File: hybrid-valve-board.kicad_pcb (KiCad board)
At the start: 2 copper layers, 68 x 79 mm, 42 parts, among them J1 XV Supply, J10 ARM, J2 MCU Supply, J3 XV In, J4 XV In, J5 XV In, J6 Continuity, J7 XV Out, J8 XV Out, J9 XV Out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

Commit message: Warranty text
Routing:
- net /XV7_PWR: track 22.5 -> 25.6 mm

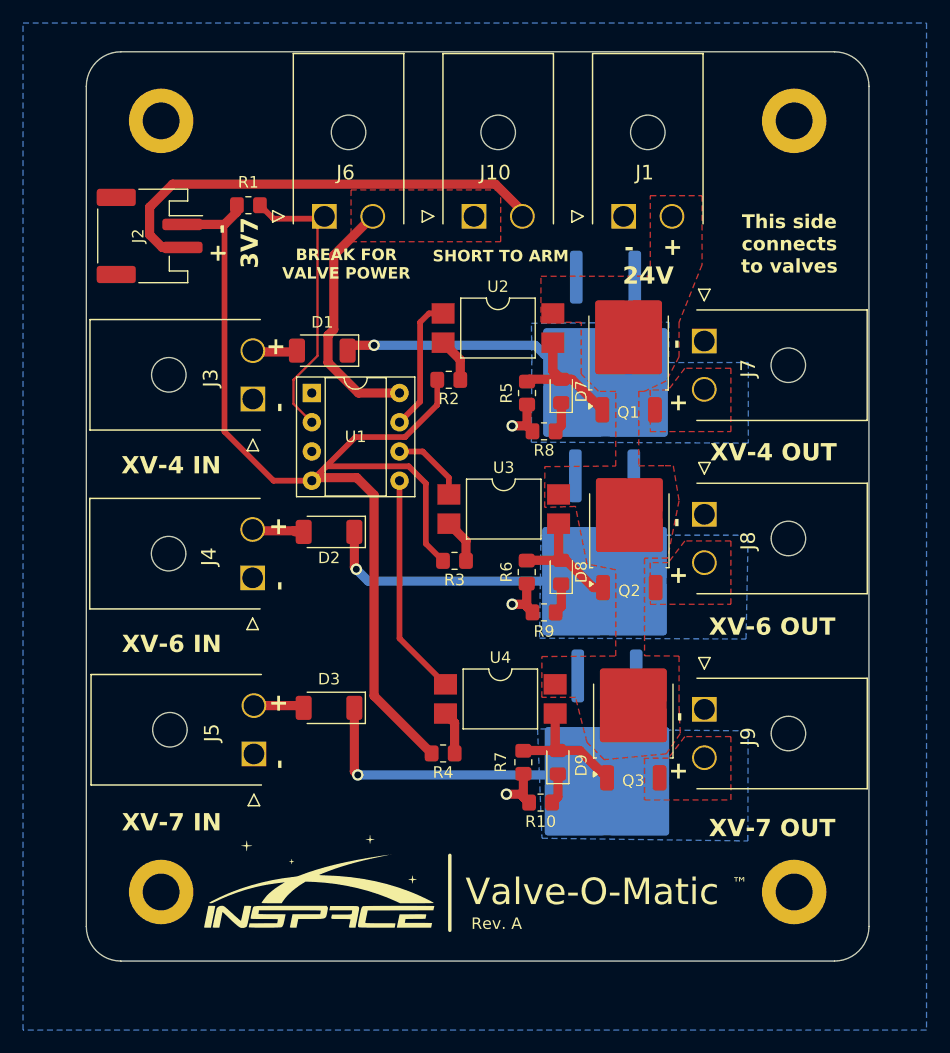
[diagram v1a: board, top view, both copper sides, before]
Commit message: Added: reverse polarity protection for MCU, arming LED and PMOS switching
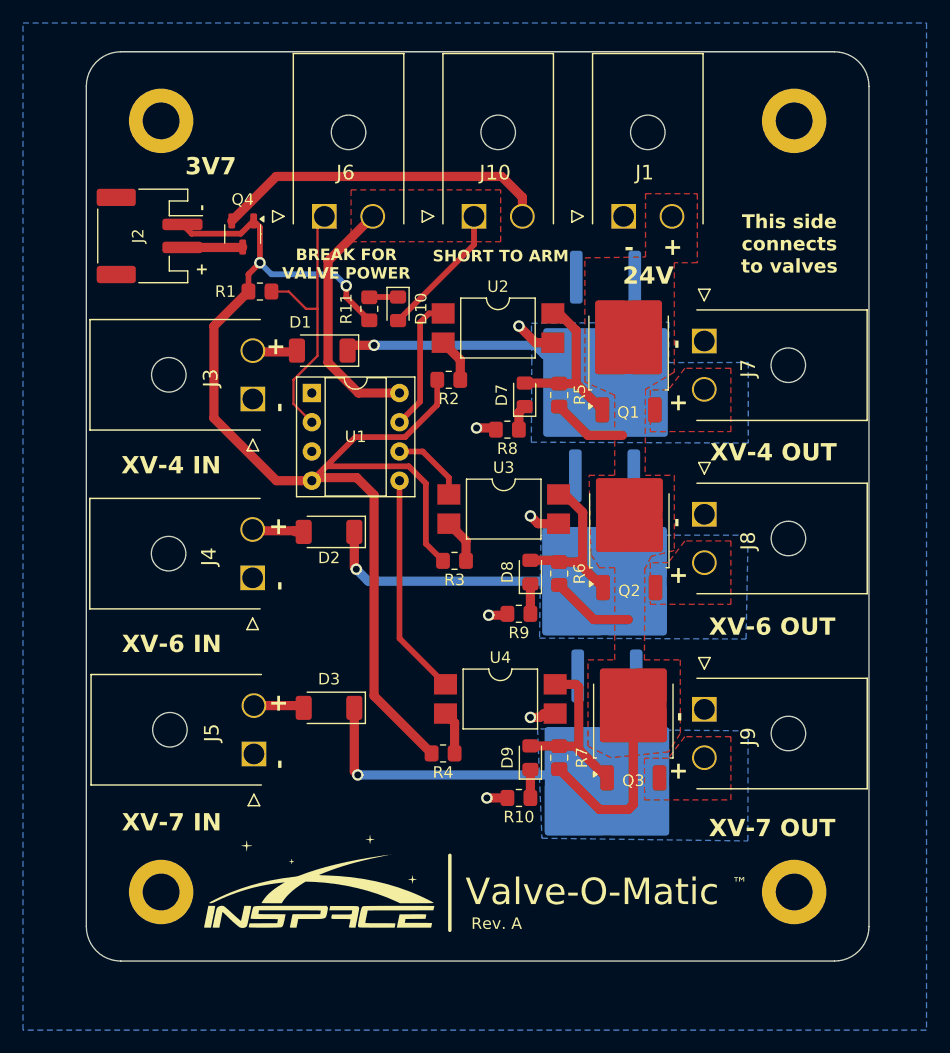
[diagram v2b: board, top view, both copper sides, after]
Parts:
- added D10: GREEN, LED_SMD:LED_0805_2012Metric_Pad1.15x1.40mm_HandSolder, F.Cu at (127.5, 86.5)
- added Q4: PMOS, Package_TO_SOT_SMD:SOT-23-3, F.Cu at (114.0, 80.0)
- added R11: 150R, Resistor_SMD:R_0805_2012Metric_Pad1.20x1.40mm_HandSolder, F.Cu at (125.0, 86.5)
- Q1, Q2, Q3: value NMOS -> PMOS
- moved R1 7.57 mm to (115.5, 85.0)
- moved D7 3.20 mm to (138.5, 94.0)
- moved R8 3.18 mm to (137.0, 97.0)
- moved R7 3.14 mm to (141.5, 125.5), turned to 90 degrees
- moved R6 2.82 mm to (141.5, 109.5), turned to 90 degrees
- moved R5 2.80 mm to (141.5, 94.0), turned to 90 degrees
- moved D8 2.68 mm to (139.0, 109.4)
- moved D9 2.42 mm to (139.0, 125.5)
- moved R9 2.18 mm to (138.0, 113.0)
- moved R10 1.93 mm to (138.0, 129.0)
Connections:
- J10 pad 2: VBAT -> VPROT
- R5 pad 1: /XV4_ON_24V -> +24VBAT
- R5 pad 2: GND -> /XV4_ON_24V
- R6 pad 1: /XV6_ON_24V -> +24VBAT
- R6 pad 2: GND -> /XV6_ON_24V
- R7 pad 1: /XV7_ON_24V -> +24VBAT
- R7 pad 2: GND -> /XV7_ON_24V
- U2 pad 3: /XV4_ON_24V -> GND
- U2 pad 4: +24VBAT -> /XV4_ON_24V
- U3 pad 3: /XV6_ON_24V -> GND
- U3 pad 4: +24VBAT -> /XV6_ON_24V
- U4 pad 3: /XV7_ON_24V -> GND
- U4 pad 4: +24VBAT -> /XV7_ON_24V
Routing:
- net VBAT: track 40.3 -> 5.25 mm
- net +24VBAT: track 0.00 -> 30.5 mm
- net VPROT: track 0.00 -> 29.7 mm
- net MCU_GND: track 98.0 -> 113.8 mm, vias 0 -> 2
- net +3V3: track 21.6 -> 33.4 mm
- net /XV6_ON_24V: track 10.9 -> 14.8 mm
- net /XV7_ON_24V: track 11.6 -> 15.4 mm
- net /XV4_ON_24V: track 11.2 -> 15.0 mm
- net Net-(D10-K): track 0.00 -> 2.51 mm
- net /CONT_IN: track 25.5 -> 24.3 mm
- net GND: track 12.8 -> 13.4 mm, vias 3 -> 6
